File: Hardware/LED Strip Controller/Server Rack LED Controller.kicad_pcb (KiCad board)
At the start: 2 copper layers, 155 parts, among them J1 Conn_01x03_Male, J10 Conn_01x03_Female, J10 UART, J11 CONN_2, J12 Conn_01x03_Male, J13 CONN_3, J14 Conn_01x03_Male, J15 Conn_01x06_Female, J16 CONN_4, J17 TST, J18 Conn_01x02_Female, J18 Conn_01x03_Male, J19 Conn_01x03_Male, J2 Screw_Terminal_01x02, J3 PWR_SWITCH, J4 Conn_02x03_Odd_Even, J5 Conn_01x03_Female, J6 CONN_1, J7 Conn_01x03_Male, J8 SWD, J9 USB_B_Micro, P1 USB_C_Plug, Q1 IRF510N, Q10 IRF510N, Q11 IRF510N, Q12 IRF510N, Q13 IRF510N, Q14 IRF510N, Q2 IRF510N, Q3 Q_PMOS_SDG, Q4 IRF510N, Q5 IRF510N, Q6 IRF510N, Q7 IRF510N, Q8 IRF510N, Q9 IRF510N, SW1 SW_Push_Dual, U1 STM32F103C8Tx, U2 LM2596S-5, U3 LD1117S50TR_SOT223, U5 INA169, U6 USBLC6-2SC6

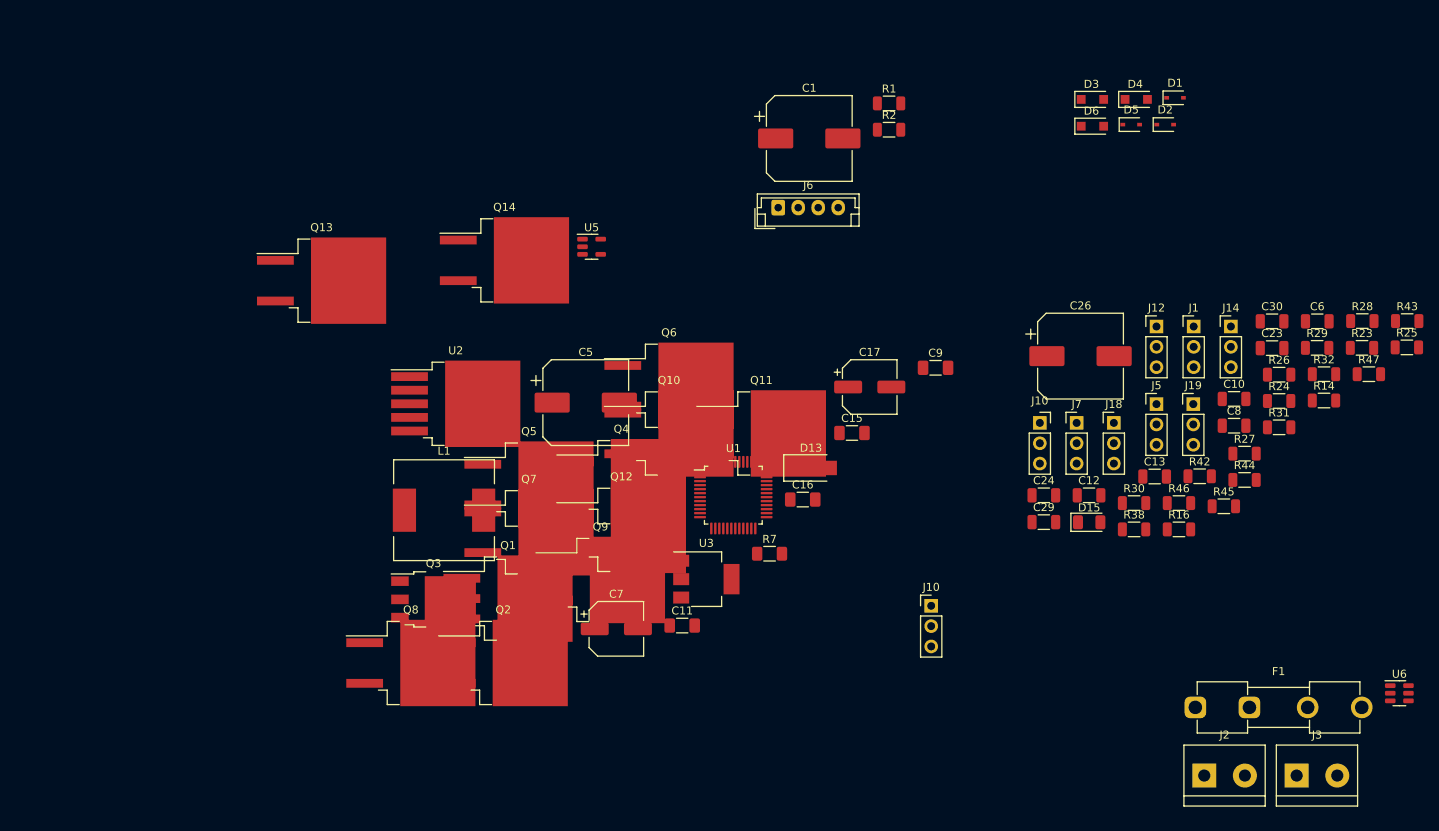
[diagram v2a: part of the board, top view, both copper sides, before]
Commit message: Adding Kicad Schematic progress
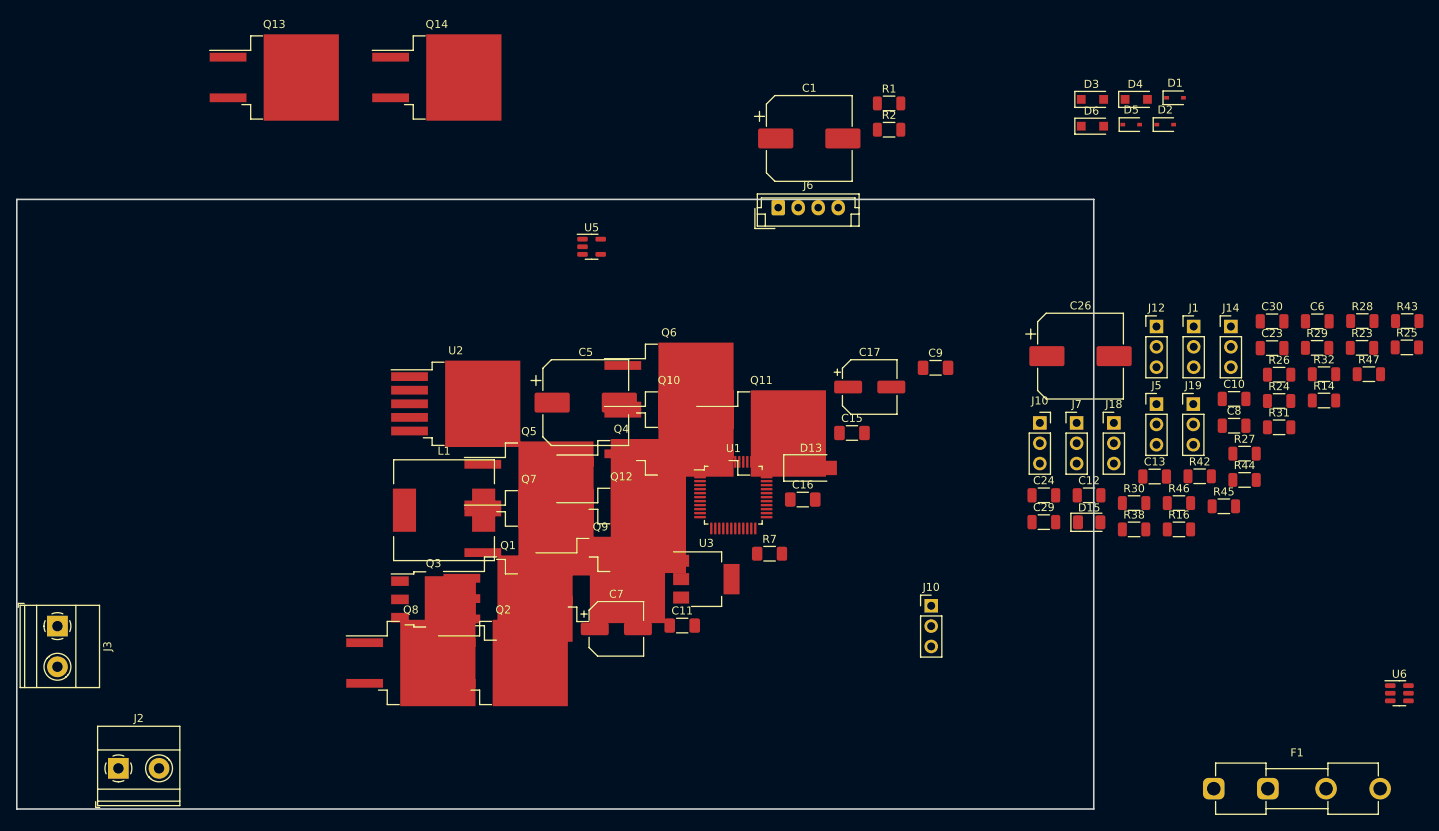
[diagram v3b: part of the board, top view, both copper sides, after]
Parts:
- J2, J3: footprint TerminalBlock:TerminalBlock_bornier-2_P5.08mm -> TerminalBlock_Phoenix:TerminalBlock_Phoenix_MKDS-1,5-2-5.08_1x02_P5.08mm_Horizontal
- moved J3 156.0 mm to (33.0, 88.9), turned to -90 degrees
- moved J2 135.7 mm to (40.6, 106.7)
- moved Q13 26.1 mm to (60.1, 20.3)
- moved Q14 24.4 mm to (80.4, 20.3)
- moved F1 10.4 mm to (177.6, 109.2)
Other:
- board outline added: 134.6 x 76.2 mm

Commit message: Started layout of PCB
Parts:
- added C100: 100uF, Capacitor_SMD:CP_Elec_6.3x7.7, F.Cu at (186.9, 146.6)
- added C35: 10nF, Capacitor_SMD:C_1206_3216Metric_Pad1.33x1.80mm_HandSolder, F.Cu at (186.6, 139.2)
- added C36: 100nF, Capacitor_SMD:C_1206_3216Metric_Pad1.33x1.80mm_HandSolder, F.Cu at (186.6, 141.8)
- added C37: 10nF, Capacitor_SMD:C_1206_3216Metric_Pad1.33x1.80mm_HandSolder, F.Cu at (166.7, 139.5)
- added C38: 100nF, Capacitor_SMD:C_1206_3216Metric_Pad1.33x1.80mm_HandSolder, F.Cu at (166.7, 141.9)
- added C39: 100uF, Capacitor_SMD:CP_Elec_6.3x7.7, F.Cu at (166.8, 146.8)
- added C40: 100uF, Capacitor_SMD:CP_Elec_10x10.5, F.Cu at (175.3, 116.8)
- added J19: Conn_02x04_Odd_Even, Connector_PinHeader_2.54mm:PinHeader_2x04_P2.54mm_Vertical, F.Cu at (185.4, 152.4)
- added J20: Conn_02x04_Odd_Even, Connector_PinHeader_2.54mm:PinHeader_2x04_P2.54mm_Vertical, F.Cu at (165.5, 152.4)
- moved R36 249.4 mm to (31.8, 108.1)
- moved R34 243.9 mm to (33.6, 115.6)
- moved R35 237.6 mm to (36.5, 108.1)
- moved D27 232.6 mm to (59.0, -32.9), turned to 180 degrees
- moved D26 228.5 mm to (65.1, -35.8), turned to 180 degrees
- moved R33 216.7 mm to (40.6, 111.8), turned to 90 degrees
- moved C28 214.9 mm to (32.5, 111.9), turned to -90 degrees
- moved R40 177.9 mm to (125.1, 148.5), turned to 180 degrees
- moved D24 171.6 mm to (135.9, -33.6), turned to 180 degrees
- moved D25 156.9 mm to (147.3, -38.1), turned to 180 degrees
- moved R28 156.6 mm to (60.2, -27.0), turned to -90 degrees
- moved R26 154.3 mm to (59.1, -30.7), turned to 180 degrees
- moved R41 153.8 mm to (128.8, 149.7), turned to -90 degrees
- moved J18 145.0 mm to (141.0, 138.3), turned to -90 degrees
- moved Q14 141.8 mm to (138.8, 149.6)
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
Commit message: Adding updated Layout, still need to finish it off, but parts are paired
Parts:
- removed P1: USB_C_Plug, Connector_USB:USB_C_Receptacle_GCT_USB4085
- removed R46, R47: 20R, Resistor_SMD:R_1206_3216Metric
- J10: value Conn_01x03_Female -> UART; footprint Connector_PinSocket_2.54mm:PinSocket_1x03_P2.54mm_Vertical -> Connector_PinHeader_2.54mm:PinHeader_1x03_P2.54mm_Vertical
- J15: value Conn_01x06_Female -> Conn_01x06_Male
- J18: value Conn_01x03_Male -> Conn_01x02_Female; footprint Connector_PinHeader_2.54mm:PinHeader_1x03_P2.54mm_Vertical -> Connector_JST:JST_EH_B2B-EH-A_1x02_P2.50mm_Vertical
- J19: value Conn_01x03_Male -> Conn_02x04_Odd_Even; footprint Connector_PinHeader_2.54mm:PinHeader_1x03_P2.54mm_Vertical -> Connector_PinHeader_2.54mm:PinHeader_2x04_P2.54mm_Vertical
- moved U3 307.6 mm to (419.1, 42.6), turned to -90 degrees
- moved D23 271.2 mm to (57.0, -93.4), turned to 180 degrees
- moved C27 270.3 mm to (487.7, 48.3), turned to -90 degrees
- moved R42 262.8 mm to (367.0, 250.5), turned to -90 degrees
- moved Q1 260.9 mm to (281.1, -91.4)
- moved R38 257.9 mm to (408.9, 167.6)
- moved R43 257.7 mm to (364.5, 250.5), turned to -90 degrees
- moved Q2 257.5 mm to (281.1, -77.6)
- moved D28 255.8 mm to (73.7, -96.5)
- moved R44 255.0 mm to (362.1, 250.5), turned to 90 degrees
- moved C25 245.4 mm to (485.1, 48.3), turned to -90 degrees
- moved D14 237.6 mm to (114.6, -96.8), turned to 180 degrees
- moved C22 237.6 mm to (477.5, 48.3), turned to -90 degrees
- moved J9 236.9 mm to (365.8, 256.5)
- moved D22 229.3 mm to (447.0, 50.8), turned to 90 degrees
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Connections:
- net Net-(J9-Pad2) renamed /D-
- net Net-(J9-Pad3) renamed /D+
- J18 pad 1: STM32_USB_C+ -> PWR_5V
- J18 pad 2: STM32_USB+ -> Net-(D30-Pad1)
- J19 pad 1: STM32_USB_C+ -> CURR_SENSE
- J19 pad 2: STM32_USB- -> +5V
- J19 pad 3: STM32_USB_MICRO- -> CURR_SENSE
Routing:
- net Net-(D26-Pad1): track 0.00 -> 31.1 mm
- net Net-(D28-Pad1): track 0.00 -> 16.9 mm
- net Net-(D25-Pad1): track 0.00 -> 14.2 mm

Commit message: Adding Fuse Holder and updating Kicad Schematic with new PSU connecotors, also started doing some of the layout
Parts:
- removed the J18 at (165.1, 63.5)
- removed the J19 at (177.8, 66.0)
- added F2: 1A, Fuse:Fuseholder_Clip-5x20mm_Littelfuse_111_Inline_P20.00x5.00mm_D1.05mm_Horizontal, F.Cu at (304.8, -81.5)
- added F3: 1A, Fuse:Fuseholder_Clip-5x20mm_Littelfuse_111_Inline_P20.00x5.00mm_D1.05mm_Horizontal, F.Cu at (208.9, -87.8)
- added F4: 1A, Fuse:Fuseholder_Clip-5x20mm_Littelfuse_111_Inline_P20.00x5.00mm_D1.05mm_Horizontal, F.Cu at (145.6, -59.4)
- added F5: 1A, Fuse:Fuseholder_Clip-5x20mm_Littelfuse_111_Inline_P20.00x5.00mm_D1.05mm_Horizontal, F.Cu at (85.9, -188.8)
- added J21: Conn_01x02_Female, Connector_JST:JST_EH_B2B-EH-A_1x02_P2.50mm_Vertical, F.Cu at (353.1, -30.5)
- added J22: Screw_Terminal_01x02, TerminalBlock_Phoenix:TerminalBlock_Phoenix_MKDS-1,5-2-5.08_1x02_P5.08mm_Horizontal, F.Cu at (-71.4, -23.5)
- added Q15: Q_PMOS_SDG, Package_TO_SOT_SMD:TO-252-3_TabPin2, F.Cu at (-61.6, -21.0)
- added R46: 10K, Resistor_SMD:R_1206_3216Metric_Pad1.30x1.75mm_HandSolder, F.Cu at (-61.0, -14.0)
- added U4: LD39050PU33R, Package_DFN_QFN:DFN-6-1EP_3x3mm_P0.95mm_EP1.7x2.6mm, F.Cu at (482.6, 43.2)
- F1: footprint Fuse:Fuseholder_Clip-5x20mm_Eaton_1A5601-01_Inline_P20.80x6.76mm_D1.70mm_Horizontal -> Fuse:Fuseholder_Clip-5x20mm_Littelfuse_111_Inline_P20.00x5.00mm_D1.05mm_Horizontal
- J1: value Conn_01x03_Male -> LED_ONE_PWR; footprint Connector_PinHeader_2.54mm:PinHeader_1x03_P2.54mm_Vertical -> Connector_PinHeader_2.54mm:PinHeader_2x03_P2.54mm_Vertical
- J12: value Conn_01x03_Male -> LED_THREE_PWR; footprint Connector_PinHeader_2.54mm:PinHeader_1x03_P2.54mm_Vertical -> Connector_PinHeader_2.54mm:PinHeader_2x03_P2.54mm_Vertical
- J14: value Conn_01x03_Male -> LED_FOUR_PWR; footprint Connector_PinHeader_2.54mm:PinHeader_1x03_P2.54mm_Vertical -> Connector_PinHeader_2.54mm:PinHeader_2x03_P2.54mm_Vertical
- J7: value Conn_01x03_Male -> LED_TWO_PWR; footprint Connector_PinHeader_2.54mm:PinHeader_1x03_P2.54mm_Vertical -> Connector_PinHeader_2.54mm:PinHeader_2x03_P2.54mm_Vertical
- moved C26 102.4 mm to (71.1, -194.3), turned to 180 degrees
- moved J14 97.8 mm to (93.3, -176.5)
- moved R28 95.9 mm to (58.4, -152.4)
- moved Q13 94.8 mm to (68.5, -152.4)
- moved R27 94.5 mm to (58.4, -167.6)
- moved Q12 94.5 mm to (68.5, -167.6)
- moved Q11 94.0 mm to (68.5, -182.9)
- moved R25 93.3 mm to (55.9, -167.6), turned to -90 degrees
- moved R24 93.1 mm to (58.4, -182.9)
- moved R26 92.3 mm to (55.9, -152.4), turned to -90 degrees
- moved R23 92.0 mm to (55.9, -182.9), turned to -90 degrees
- moved D24 91.2 mm to (53.3, -167.6), turned to -90 degrees
- moved D27 90.2 mm to (53.3, -152.4), turned to -90 degrees
- moved D23 89.5 mm to (53.3, -182.9), turned to -90 degrees
- moved J16 81.3 mm to (84.1, -162.6)
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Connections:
- C1 pad 2: CURR_SENSE -> GND
- C10 pad 2: CURR_SENSE -> GND
- C100 pad 2: CURR_SENSE -> GND
- C11 pad 2: CURR_SENSE -> GND
- C12 pad 2: CURR_SENSE -> GND
- C13 pad 2: CURR_SENSE -> GND
- C14 pad 2: CURR_SENSE -> GND
- C15 pad 2: CURR_SENSE -> GND
- C16 pad 2: CURR_SENSE -> GND
- C17 pad 2: CURR_SENSE -> GND
- C18 pad 2: CURR_SENSE -> GND
- C19 pad 2: CURR_SENSE -> GND
- C2 pad 2: CURR_SENSE -> GND
- C20 pad 2: CURR_SENSE -> GND
- C21 pad 2: CURR_SENSE -> GND
- C22 pad 2: CURR_SENSE -> GND
- C23 pad 2: CURR_SENSE -> GND
- C24 pad 2: CURR_SENSE -> GND
- C25 pad 2: CURR_SENSE -> GND
- C26 pad 2: CURR_SENSE -> GND
- C27 pad 2: CURR_SENSE -> GND
- C28 pad 2: CURR_SENSE -> GND
- C29 pad 2: CURR_SENSE -> GND
- C3 pad 2: CURR_SENSE -> GND
- C30 pad 2: CURR_SENSE -> GND
- C31 pad 2: CURR_SENSE -> GND
- C32 pad 2: CURR_SENSE -> GND
- C33 pad 2: CURR_SENSE -> GND
- C34 pad 2: CURR_SENSE -> GND
- C35 pad 1: CURR_SENSE -> GND
- C36 pad 2: CURR_SENSE -> GND
- C37 pad 1: CURR_SENSE -> GND
- C38 pad 2: CURR_SENSE -> GND
- C39 pad 2: CURR_SENSE -> GND
- C4 pad 2: CURR_SENSE -> GND
- C40 pad 2: CURR_SENSE -> GND
- C5 pad 2: CURR_SENSE -> GND
- C6 pad 2: CURR_SENSE -> GND
- C7 pad 2: CURR_SENSE -> GND
- C8 pad 2: CURR_SENSE -> GND
- C9 pad 2: CURR_SENSE -> GND
- D13 pad 2: CURR_SENSE -> GND
- D15 pad 1: CURR_SENSE -> GND
- D22 pad 1: CURR_SENSE -> GND
- D29 pad 1: CURR_SENSE -> GND
- J1 pad 2: CONN_1_5V -> PWR_5V
- J1 pad 3: EXT_5V -> CONN_1_5V
- J10 pad 3: CURR_SENSE -> GND (x2)
- J11 pad 1: CONN_2_5V -> Net-(J11-Pad1)
- J12 pad 2: CONN_3_5V -> PWR_5V
- J12 pad 3: EXT_5V -> CONN_3_5V
- J13 pad 1: CONN_3_5V -> Net-(J13-Pad1)
- J14 pad 2: CONN_4_5V -> PWR_5V
- J14 pad 3: EXT_5V -> CONN_4_5V
- J15 pad 6: CURR_SENSE -> GND
- J16 pad 1: CONN_4_5V -> Net-(J16-Pad1)
- J17 pad 5: CURR_SENSE -> GND
- J19 pad 1: CURR_SENSE -> GND
- J19 pad 3: CURR_SENSE -> GND
- J19 pad 5: CURR_SENSE -> GND
- J19 pad 7: CURR_SENSE -> GND
- J2 pad 2: CURR_SENSE -> GND
- J20 pad 1: CURR_SENSE -> GND
- J20 pad 3: CURR_SENSE -> GND
- J20 pad 5: CURR_SENSE -> GND
- J20 pad 7: CURR_SENSE -> GND
- J4 pad 1: CURR_SENSE -> GND
- J4 pad 2: CURR_SENSE -> GND
- J5 pad 3: CURR_SENSE -> GND
- J6 pad 1: CONN_1_5V -> Net-(J6-Pad1)
- J7 pad 2: CONN_2_5V -> PWR_5V
- J7 pad 3: EXT_5V -> CONN_2_5V
- J8 pad 4: CURR_SENSE -> GND
- J9 pad 5: CURR_SENSE -> GND
- Q1 pad 3: CURR_SENSE -> GND
- Q10 pad 3: CURR_SENSE -> GND
- Q11 pad 3: CURR_SENSE -> GND
- Q12 pad 3: CURR_SENSE -> GND
- Q13 pad 3: CURR_SENSE -> GND
- Q14 pad 3: CURR_SENSE -> GND
- Q2 pad 3: CURR_SENSE -> GND
- Q4 pad 3: CURR_SENSE -> GND
- Q5 pad 3: CURR_SENSE -> GND
- Q6 pad 3: CURR_SENSE -> GND
- Q7 pad 3: CURR_SENSE -> GND
- Q8 pad 3: CURR_SENSE -> GND
- Q9 pad 3: CURR_SENSE -> GND
- R12 pad 2: CURR_SENSE -> GND
- R13 pad 2: CURR_SENSE -> GND
- R17 pad 2: CURR_SENSE -> GND
- R2 pad 2: CURR_SENSE -> GND
- R20 pad 2: CURR_SENSE -> GND
- R21 pad 2: CURR_SENSE -> GND
- R24 pad 2: CURR_SENSE -> GND
- R27 pad 2: CURR_SENSE -> GND
- R28 pad 2: CURR_SENSE -> GND
- R34 pad 2: Net-(R34-Pad2) -> GND
- R36 pad 1: CURR_SENSE -> GND
- R41 pad 2: CURR_SENSE -> GND
- R5 pad 2: CURR_SENSE -> GND
- R6 pad 2: CURR_SENSE -> GND
- R7 pad 2: CURR_SENSE -> GND
- R9 pad 2: CURR_SENSE -> GND
- U1 pad 23: CURR_SENSE -> GND
- U1 pad 35: CURR_SENSE -> GND
- U1 pad 47: CURR_SENSE -> GND
- U1 pad 8: CURR_SENSE -> GND
- U2 pad 3: CURR_SENSE -> GND
- U2 pad 5: CURR_SENSE -> GND
- U3 pad 1: CURR_SENSE -> GND
- U5 pad 1: Net-(R34-Pad2) -> GND
- U5 pad 2: CURR_SENSE -> GND
- U6 pad 2: CURR_SENSE -> GND
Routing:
- net CONN_4_5V: track 0.00 -> 84.3 mm, vias 0 -> 3
- net PWM_4_GREEN: track 0.00 -> 38.0 mm
- net Net-(D28-Pad1): track 16.9 -> 40.2 mm
- net PWM_4_RED: track 0.00 -> 22.9 mm
- net Net-(J22-Pad1): track 0.00 -> 16.3 mm
- net Net-(D25-Pad1): track 14.2 -> 28.3 mm
- net Net-(D27-Pad1): track 0.00 -> 9.97 mm
- net Net-(D24-Pad1): track 0.00 -> 9.97 mm
- net Net-(D23-Pad1): track 0.00 -> 9.97 mm
- net Net-(D26-Pad1): track 31.1 -> 22.4 mm
- net PWM_4_BLUE: track 0.00 -> 8.15 mm
- net Net-(J16-Pad1): track 0.00 -> 6.19 mm
- net Net-(Q15-Pad1): track 0.00 -> 3.73 mm

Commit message: Adding documentation regarding C# User Interface design
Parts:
- moved C26 1.36 mm to (69.8, -194.3)
- moved D23 1.36 mm to (52.0, -182.9)
- moved D24 1.36 mm to (52.0, -167.6)
- moved D25 1.36 mm to (69.1, -160.0)
- moved D26 1.36 mm to (69.1, -144.8)
- moved D27 1.36 mm to (52.0, -152.4)
- moved D28 1.36 mm to (69.1, -175.3)
- moved F5 1.36 mm to (84.5, -188.8)
- moved J16 1.36 mm to (82.8, -162.6)
- moved Q11 1.36 mm to (67.1, -182.9)
- moved Q12 1.36 mm to (67.1, -167.6)
- moved Q13 1.36 mm to (67.1, -152.4)
- moved R23 1.36 mm to (54.5, -182.9)
- moved R24 1.36 mm to (57.1, -182.9)
- moved R25 1.36 mm to (54.5, -167.6)
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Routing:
- net CONN_4_5V: track 84.3 -> 85.3 mm
